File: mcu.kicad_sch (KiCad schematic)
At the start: 65 parts, among them J1 USB_C, P20 HEADER-2x11, P22 HEADER-2x13, P26 LPC_JTAG, P28 HEADER-2x11, SW1 SWITCH, SW2 SWITCH, U15 TVS_USB, U20 W25Q80, U23 LPC4330FET180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

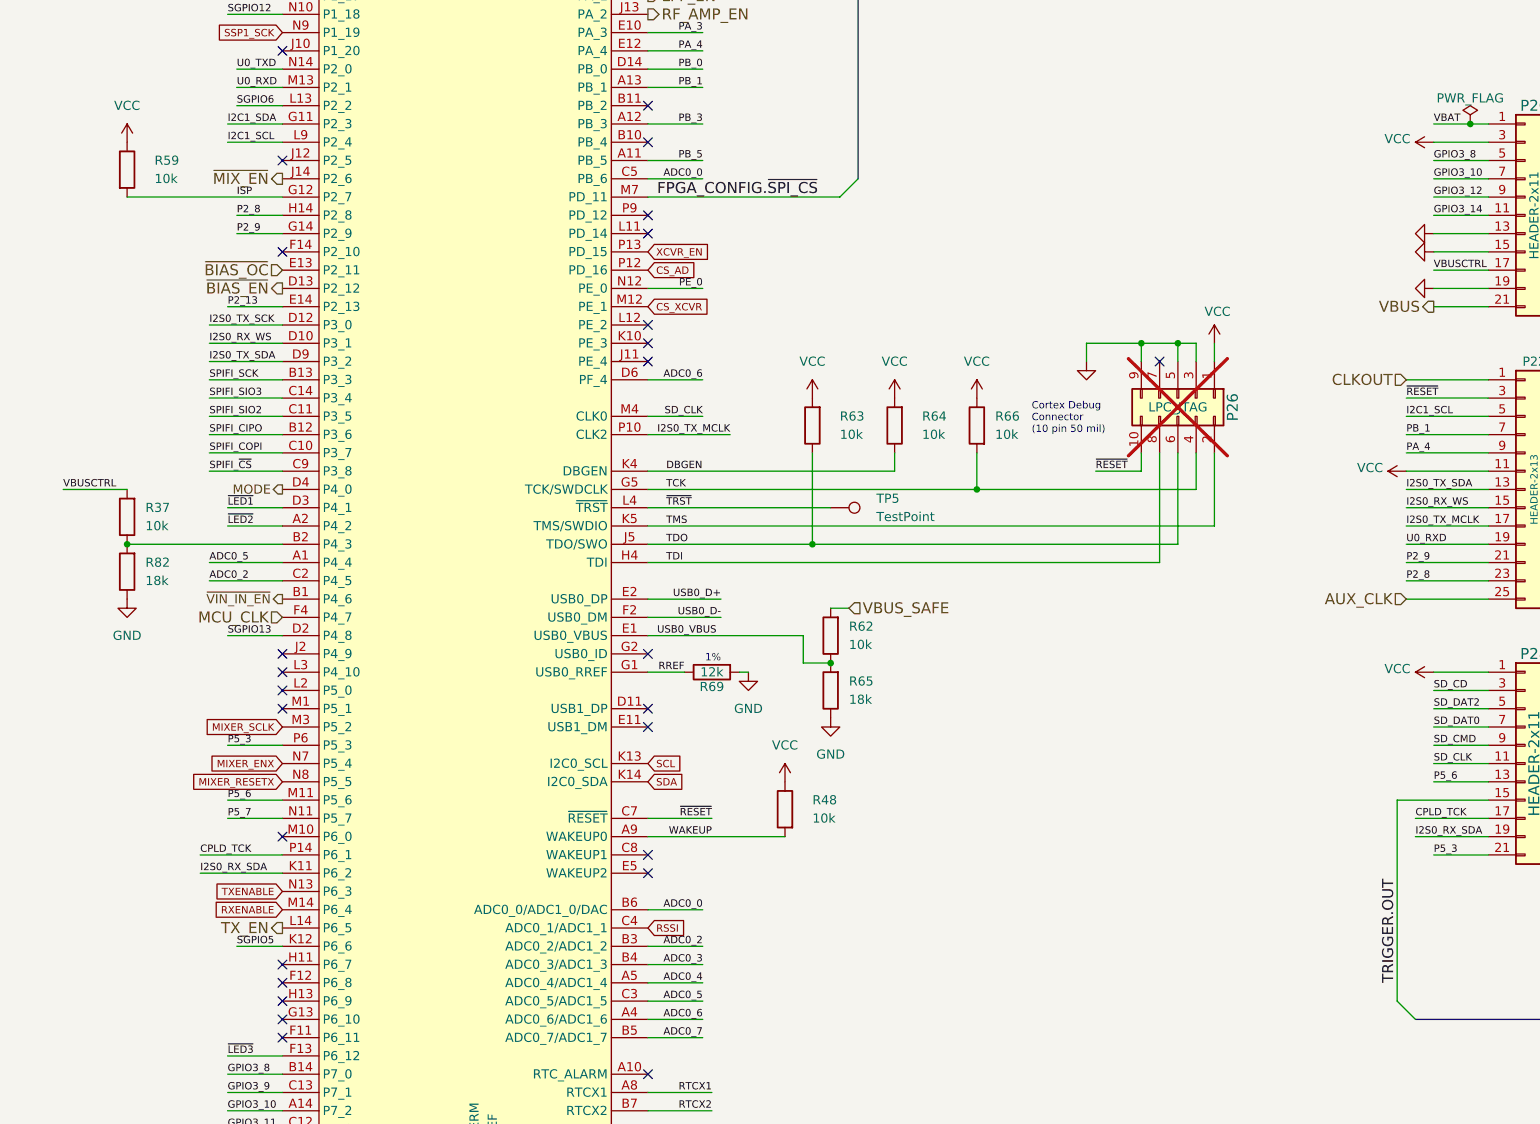
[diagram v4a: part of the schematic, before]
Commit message: Add current-limiting switch to expansion interface
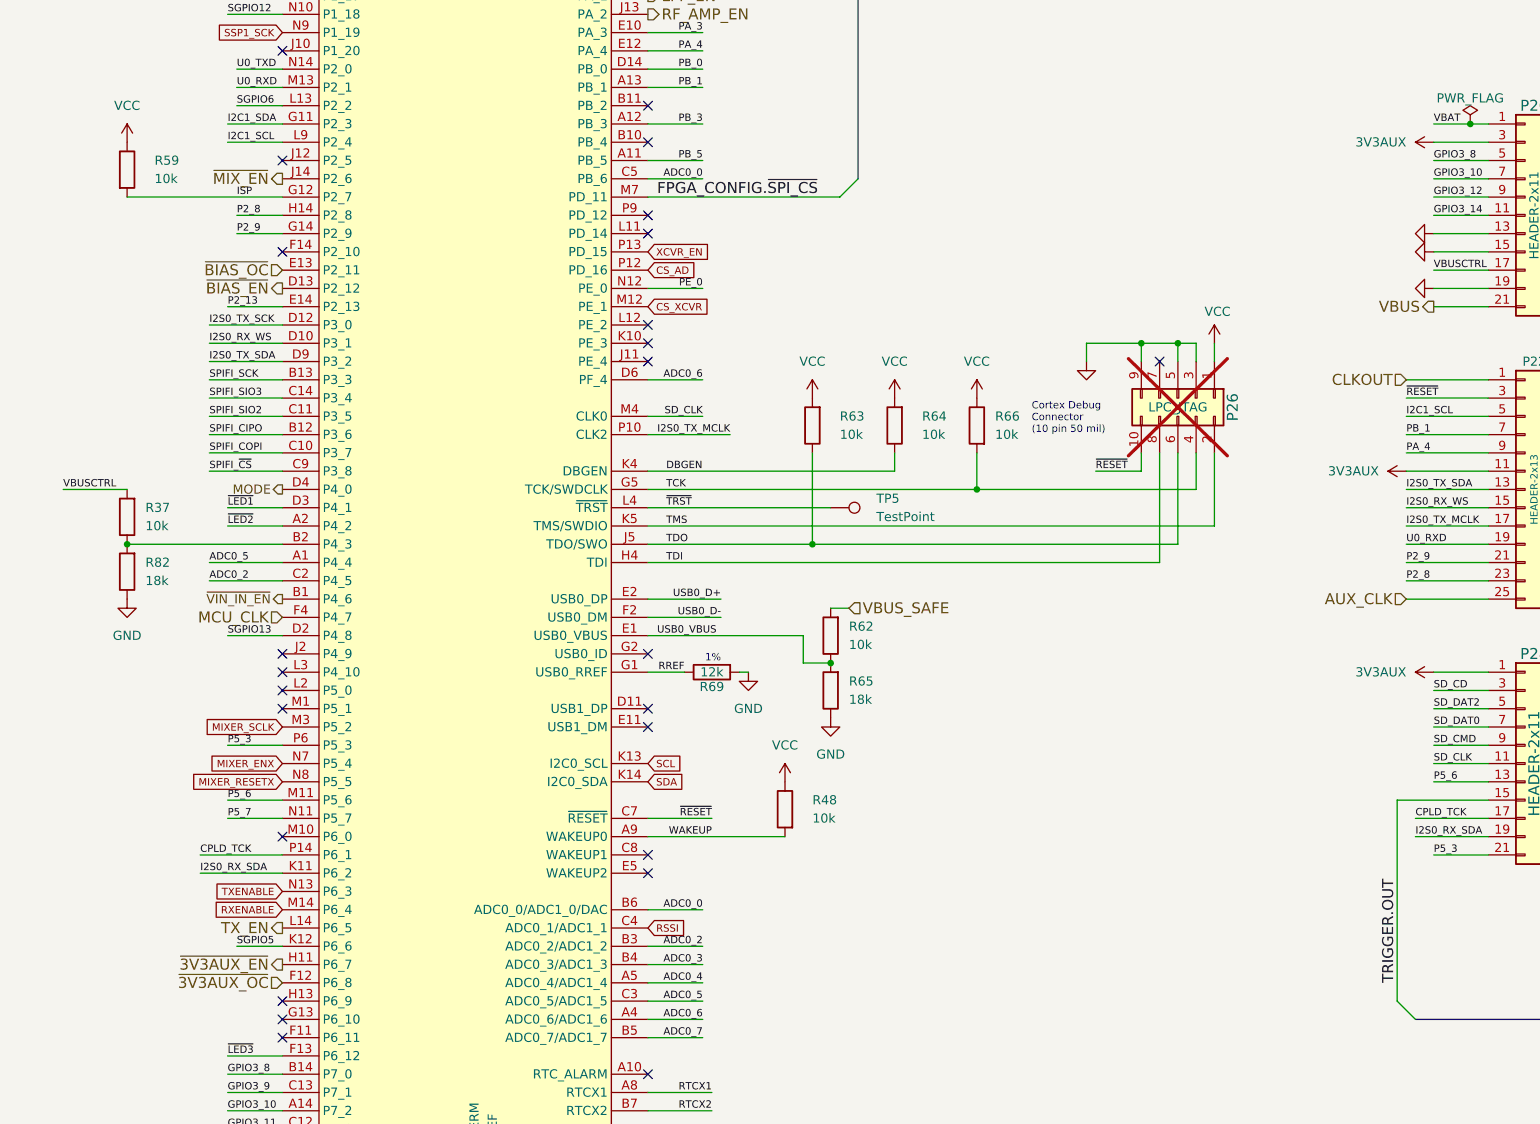
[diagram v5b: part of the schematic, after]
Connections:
- net VCC: no longer P20.3 (Pin_3), P22.11 (Pin_11), P28.1 (Pin_1)
- net ~{3V3AUX_OC}: now reaches U23.F12 (P6_8)
- net ~{3V3AUX_EN}: now reaches U23.H11 (P6_7)
- new net 3V3AUX: P20.3 (Pin_3), P22.11 (Pin_11), P28.1 (Pin_1)
- no-connect marks 36 -> 34
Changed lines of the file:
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@@
 	)
 	(no_connect
-		(at 194.31 218.44)
-	)
-	(no_connect
 		(at 245.11 175.26)
 	)
@@
 	)
 	(no_connect
-		(at 194.31 220.98)
-	)
-	(no_connect
 		(at 245.11 203.2)
 	)
@@
 		)
 	)
+	(hierarchical_label "~{3V3AUX_EN}"
+		(shape output)
+		(at 194.31 218.44 180)
+		(fields_autoplaced yes)
+		(effects
+			(font
+				(size 1.524 1.524)
+			)
+			(justify right)
+		)
+	)
 	(hierarchical_label "MCU_CLK"
 		(shape input)
@@
 		)
 	)
+	(hierarchical_label "~{3V3AUX_OC}"
+		(shape input)
+		(at 194.31 220.98 180)
+		(fields_autoplaced yes)
+		(effects
+			(font
+				(size 1.524 1.524)
+			)
+			(justify right)
+		)
+	)
 	(hierarchical_label "VBUS_SAFE"
 		(shape input)
@@
 	(symbol
 		(lib_id "power:VCC")
-		(at 350.52 149.86 90)
-		(unit 1)
-		(exclude_from_sim no)
-		(in_bom yes)
-		(on_board yes)
-		(dnp no)
-		(property "Reference" "#PWR0268"
-			(at 354.33 149.86 0)
-			(effects
-				(font
-					(size 1.27 1.27)
-				)
-				(hide yes)
-			)
-		)
-		(property "Value" "VCC"
-			(at 347.2942 149.4028 90)
-			(effects
-				(font
-					(size 1.27 1.27)
-				)
-				(justify left)
-			)
-		)
-		(property "Footprint" ""
-			(at 350.52 149.86 0)
-			(effects
-				(font
-					(size 1.27 1.27)
-				)
-				(hide yes)
-			)
-		)
-		(property "Datasheet" ""
-			(at 350.52 149.86 0)
-			(effects
-				(font
-					(size 1.27 1.27)
-				)
-				(hide yes)
-			)
-		)
-		(property "Description" "Power symbol creates a global label with name \"VCC\""
-			(at 350.52 149.86 0)
-			(effects
-				(font
-					(size 1.27 1.27)
-				)
-				(hide yes)
-			)
-		)
-		(pin "1"
-		)
-		(instances
-			(project ""
-				(path "/dba4afc6-760f-46cb-a936-032b76448f03/00000000-0000-0000-0000-00005037043e"
-					(reference "#PWR0268")
-					(unit 1)
-				)
-			)
-		)
-	)
-	(symbol
-		(lib_id "power:VCC")
-		(at 354.33 177.8 90)
-		(unit 1)
-		(exclude_from_sim no)
-		(in_bom yes)
-		(on_board yes)
-		(dnp no)
-		(property "Reference" "#PWR0306"
-			(at 358.14 177.8 0)
-			(effects
-				(font
-					(size 1.27 1.27)
-				)
-				(hide yes)
-			)
-		)
-		(property "Value" "VCC"
-			(at 351.1042 177.3428 90)
-			(effects
-				(font
-					(size 1.27 1.27)
-				)
-				(justify left)
-			)
-		)
-		(property "Footprint" ""
-			(at 354.33 177.8 0)
-			(effects
-				(font
-					(size 1.27 1.27)
-				)
-				(hide yes)
-			)
-		)
-		(property "Datasheet" ""
-			(at 354.33 177.8 0)
-			(effects
-				(font
-					(size 1.27 1.27)
-				)
-				(hide yes)
-			)
-		)
-		(property "Description" "Power symbol creates a global label with name \"VCC\""
-			(at 354.33 177.8 0)
-			(effects
-				(font
-					(size 1.27 1.27)
-				)
-				(hide yes)
-			)
-		)
-		(pin "1"
-		)
-		(instances
-			(project ""
-				(path "/dba4afc6-760f-46cb-a936-032b76448f03/00000000-0000-0000-0000-00005037043e"
-					(reference "#PWR0306")
-					(unit 1)
-				)
-			)
-		)
-	)
-	(symbol
-		(lib_id "power:VCC")
 		(at 77.47 264.16 270)
 		(unit 1)
@@
 	(symbol
 		(lib_id "power:VCC")
-		(at 354.33 104.14 90)
-		(unit 1)
-		(exclude_from_sim no)
-		(in_bom yes)
-		(on_board yes)
-		(dnp no)
-		(property "Reference" "#PWR0320"
-			(at 358.14 104.14 0)
-			(effects
-				(font
-					(size 1.27 1.27)
-				)
-				(hide yes)
-			)
-		)
-		(property "Value" "VCC"
-			(at 351.1042 103.6828 90)
-			(effects
-				(font
-					(size 1.27 1.27)
-				)
-				(justify left)
-			)
-		)
-		(property "Footprint" ""
-			(at 354.33 104.14 0)
-			(effects
-				(font
-					(size 1.27 1.27)
-				)
-				(hide yes)
-			)
-		)
-		(property "Datasheet" ""
-			(at 354.33 104.14 0)
-			(effects
-				(font
-					(size 1.27 1.27)
-				)
-				(hide yes)
-			)
-		)
-		(property "Description" "Power symbol creates a global label with name \"VCC\""
-			(at 354.33 104.14 0)
-			(effects
-				(font
-					(size 1.27 1.27)
-				)
-				(hide yes)
-			)
-		)
-		(pin "1"
-		)
-		(instances
-			(project ""
-				(path "/dba4afc6-760f-46cb-a936-032b76448f03/00000000-0000-0000-0000-00005037043e"
-					(reference "#PWR0320")
-					(unit 1)
-				)
-			)
-		)
-	)
-	(symbol
-		(lib_id "power:VCC")
 		(at 323.85 132.08 0)
 		(unit 1)
@@
 	)
 	(symbol
+		(lib_id "praline:3V3AUX")
+		(at 350.52 149.86 90)
+		(unit 1)
+		(exclude_from_sim no)
+		(in_bom yes)
+		(on_board yes)
+		(dnp no)
+		(fields_autoplaced yes)
+		(property "Reference" "#PWR0239"
+			(at 354.33 149.86 0)
+			(effects
+				(font
+					(size 1.27 1.27)
+				)
+				(hide yes)
+			)
+		)
+		(property "Value" "3V3AUX"
+			(at 346.71 149.8599 90)
+			(effects
+				(font
+					(size 1.27 1.27)
+				)
+				(justify left)
+			)
+		)
+		(property "Footprint" ""
+			(at 350.52 149.86 0)
+			(effects
+				(font
+					(size 1.27 1.27)
+				)
+				(hide yes)
+			)
+		)
+		(property "Datasheet" ""
+			(at 350.52 149.86 0)
+			(effects
+				(font
+					(size 1.27 1.27)
+				)
+				(hide yes)
+			)
+		)
+		(property "Description" "Power symbol creates a global label with name \"3V3AUX\""
+			(at 350.52 149.86 0)
+			(effects
+				(font
+					(size 1.27 1.27)
+				)
+				(hide yes)
+			)
+		)
+		(pin "1"
+		)
+		(instances
+			(project "praline"
+				(path "/dba4afc6-760f-46cb-a936-032b76448f03/00000000-0000-0000-0000-00005037043e"
+					(reference "#PWR0239")
+					(unit 1)
+				)
+			)
+		)
+	)
+	(symbol
 		(lib_id "power:VCC")
 		(at 264.16 193.04 0)
@@
 	)
 	(symbol
+		(lib_id "praline:3V3AUX")
+		(at 354.33 177.8 90)
+		(unit 1)
+		(exclude_from_sim no)
+		(in_bom yes)
+		(on_board yes)
+		(dnp no)
+		(fields_autoplaced yes)
+		(property "Reference" "#PWR0238"
+			(at 358.14 177.8 0)
+			(effects
+				(font
+					(size 1.27 1.27)
+				)
+				(hide yes)
+			)
+		)
+		(property "Value" "3V3AUX"
+			(at 350.52 177.7999 90)
+			(effects
+				(font
+					(size 1.27 1.27)
+				)
+				(justify left)
+			)
+		)
+		(property "Footprint" ""
+			(at 354.33 177.8 0)
+			(effects
+				(font
+					(size 1.27 1.27)
+				)
+				(hide yes)
+			)
+		)
+		(property "Datasheet" ""
+			(at 354.33 177.8 0)
+			(effects
+				(font
+					(size 1.27 1.27)
+				)
+				(hide yes)
+			)
+		)
+		(property "Description" "Power symbol creates a global label with name \"3V3AUX\""
+			(at 354.33 177.8 0)
+			(effects
+				(font
+					(size 1.27 1.27)
+				)
+				(hide yes)
+			)
+		)
+		(pin "1"
+		)
+		(instances
+			(project "praline"
+				(path "/dba4afc6-760f-46cb-a936-032b76448f03/00000000-0000-0000-0000-00005037043e"
+					(reference "#PWR0238")
+					(unit 1)
+				)
+			)
+		)
+	)
+	(symbol
 		(lib_id "Device:R")
 		(at 60.96 104.14 180)
@@
 					(unit 1)
 				)
+			)
+		)
+	)
+	(symbol
+		(lib_id "praline:3V3AUX")
+		(at 354.33 104.14 90)
+		(unit 1)
+		(exclude_from_sim no)
+		(in_bom yes)
+		(on_board yes)
+		(dnp no)
+		(fields_autoplaced yes)
+		(property "Reference" "#PWR0240"
+			(at 358.14 104.14 0)
+			(effects
+				(font
+					(size 1.27 1.27)
+				)
+				(hide yes)
+			)
+		)
+		(property "Value" "3V3AUX"
+			(at 350.52 104.1399 90)
+			(effects
+				(font
+					(size 1.27 1.27)
+				)
+				(justify left)
+			)
+		)
+		(property "Footprint" ""
+			(at 354.33 104.14 0)
+			(effects
+				(font
+					(size 1.27 1.27)
+				)
+				(hide yes)
+			)
+		)
+		(property "Datasheet" ""
+			(at 354.33 104.14 0)
+			(effects
+				(font
+					(size 1.27 1.27)
+				)
+				(hide yes)
+			)
+		)
+		(property "Description" "Power symbol creates a global label with name \"3V3AUX\""
+			(at 354.33 104.14 0)
+			(effects
+				(font
+					(size 1.27 1.27)
+				)
+				(hide yes)
+			)
+		)
+		(pin "1"
+		)
+		(instances
+			(project "praline"
+				(path "/dba4afc6-760f-46cb-a936-032b76448f03/00000000-0000-0000-0000-00005037043e"
+					(reference "#PWR0240")
+					(unit 1)
+				)

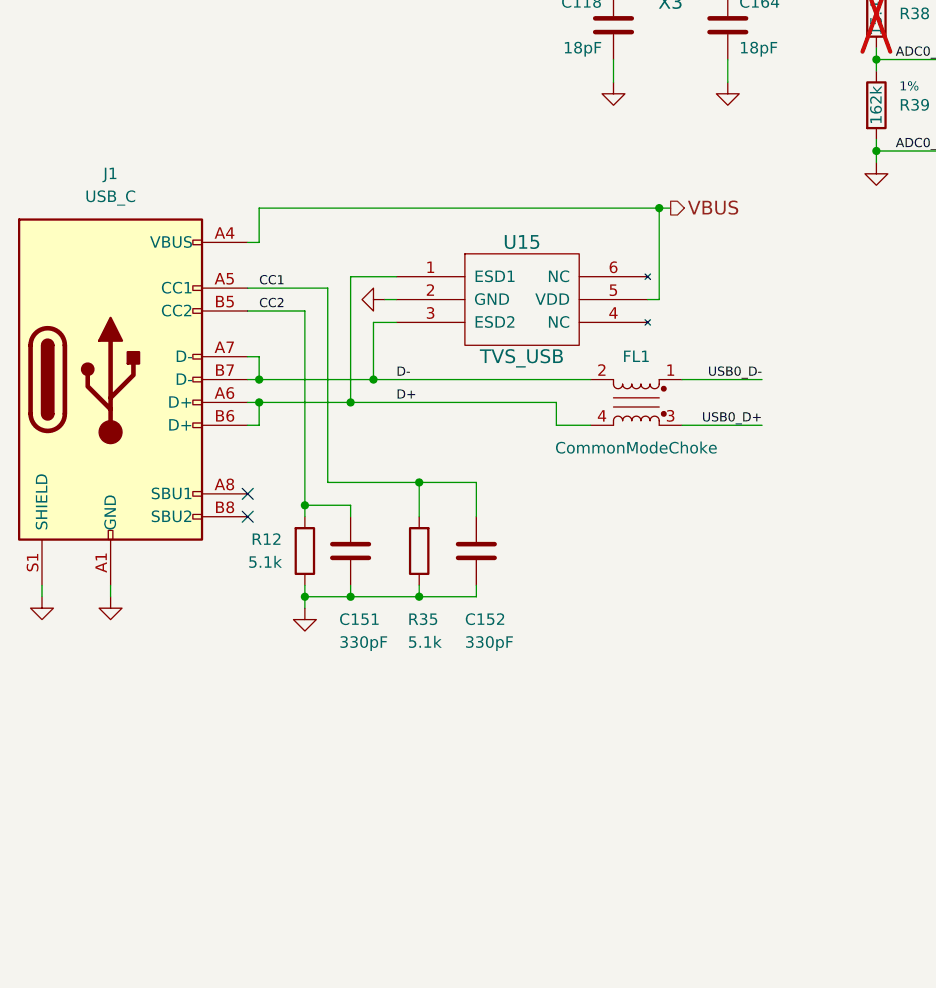
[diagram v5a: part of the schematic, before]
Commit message: Update USB D+/D- TVS and improve routing
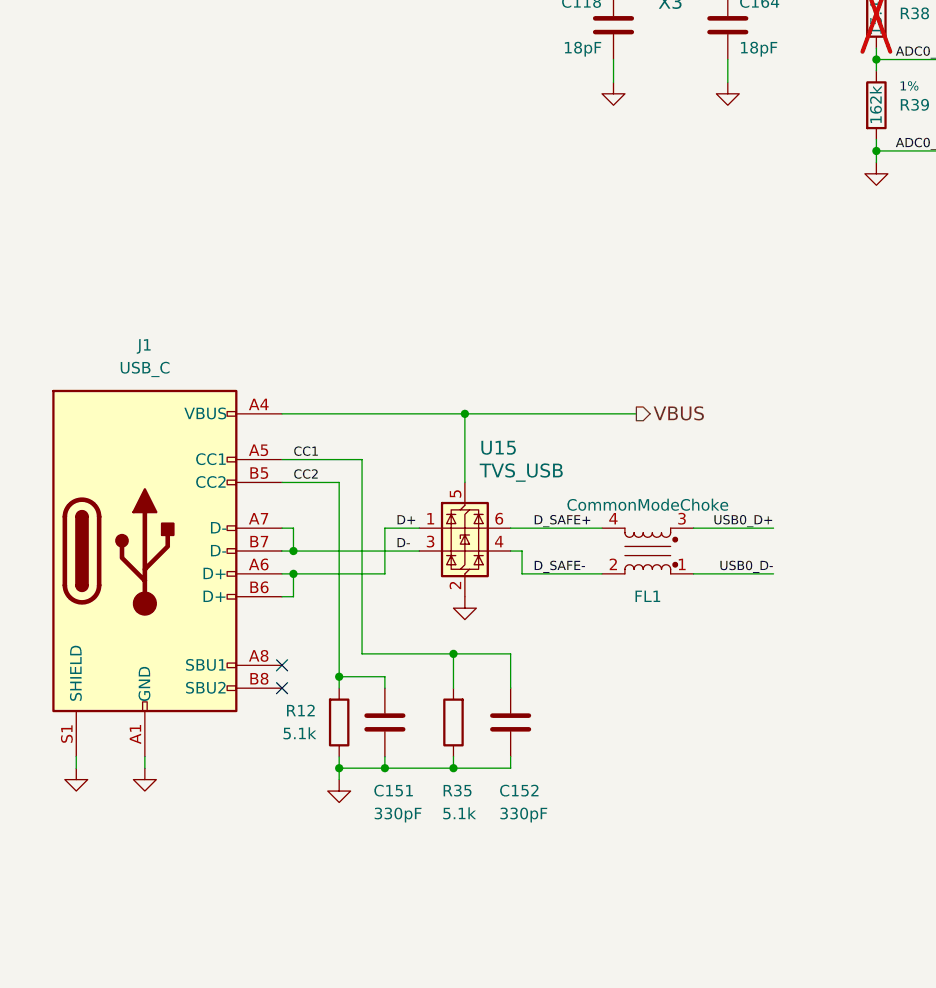
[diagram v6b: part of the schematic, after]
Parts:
- U15: footprint hackrf:GSG-LXES1TBCC2-004 -> Package_TO_SOT_SMD:SOT-563; symbol hackrf:LXES1TBCC2-004 -> Power_Protection:USBLC6-2P6; Manufacturer Vishay -> UMW; Part Number VBUS54CV-HSF-G4-08 -> USBLC6-2P6
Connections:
- net D+: no longer FL1.4
- net D-: no longer FL1.2
- net D_SAFE-: now reaches U15.4 (I/O2)
- net D_SAFE-: now also FL1.2
- net D_SAFE+: now reaches U15.6 (I/O1)
- net D_SAFE+: now also FL1.4
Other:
- moved on the sheet: C151, C152, FL1, J1, R12, R35
